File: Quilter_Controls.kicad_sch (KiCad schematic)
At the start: 16 parts, among them J1 Conn_01x10_Male, J10 Conn_01x04_Male, J2 Conn_01x10_Male, J3 Conn_01x10_Male, J4 Audio_In, J5 Audio_Out, J6 Audio_Mix, J7 Freq_V_Oct, J8 Freq_CV, J9 Conn_02x04_Top_Bottom

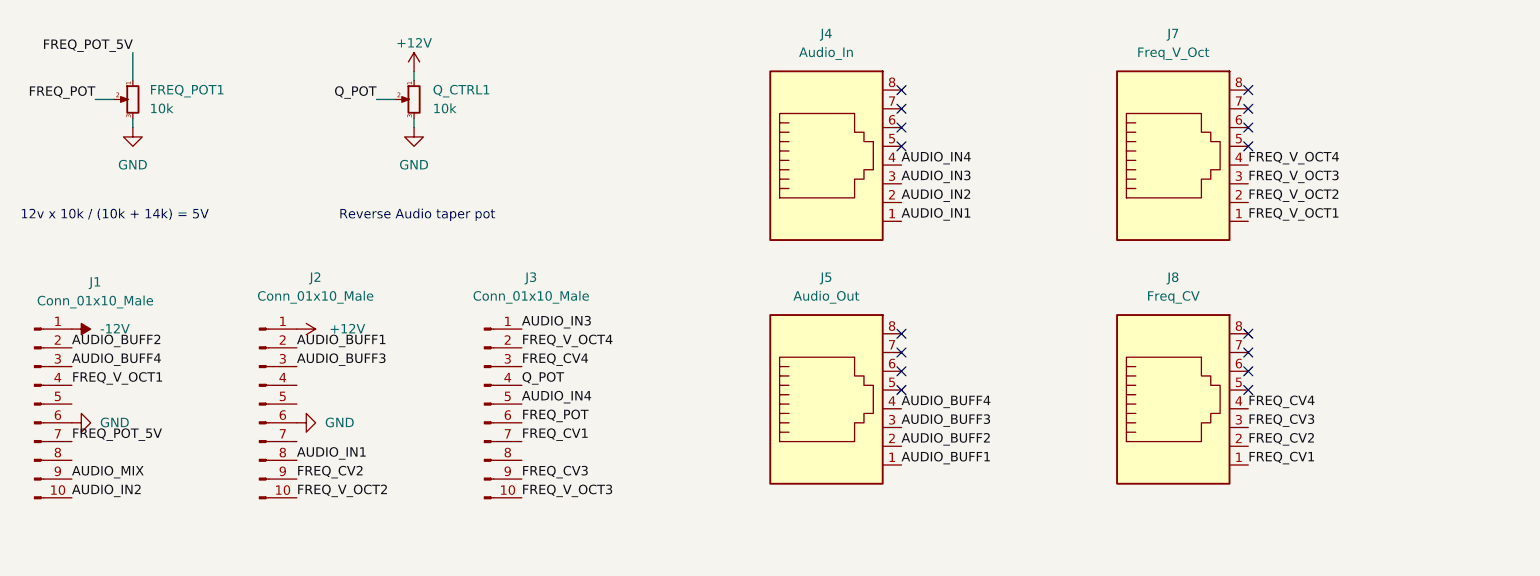
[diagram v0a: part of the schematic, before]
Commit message: Added all voice filter CV; panel draft done
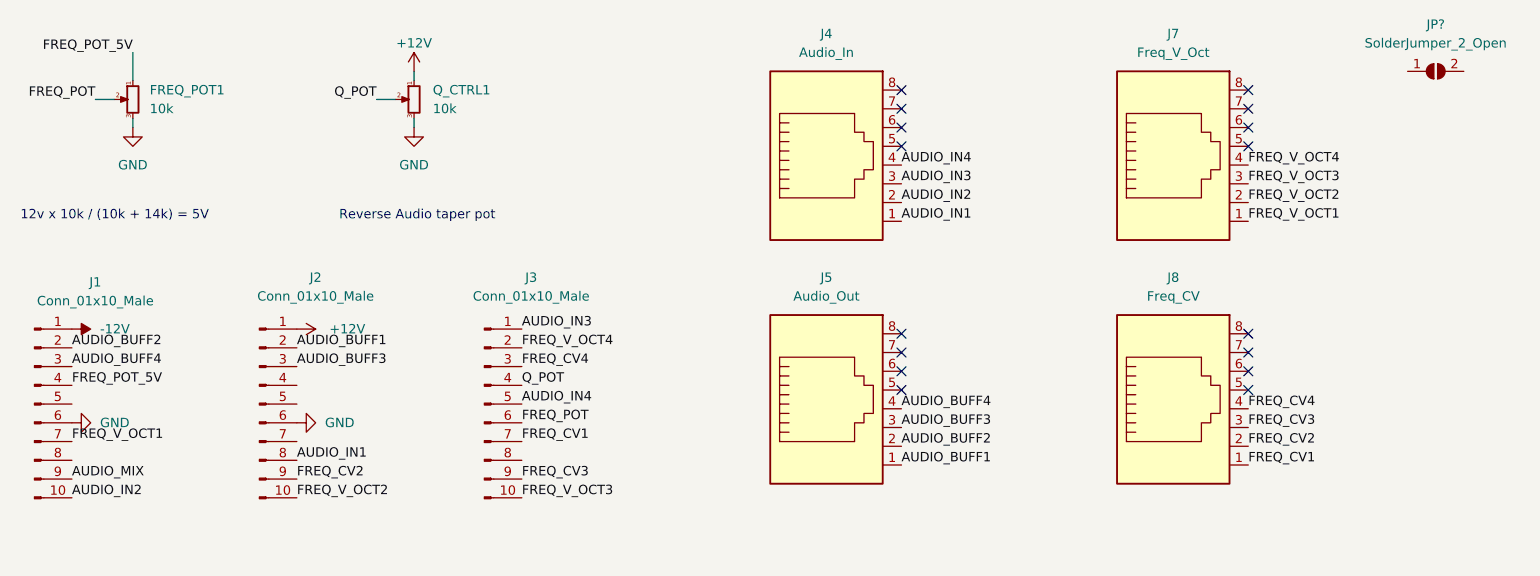
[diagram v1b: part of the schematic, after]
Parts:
- added JP?: SolderJumper_2_Open, symbol Jumper:SolderJumper_2_Open
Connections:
- net FREQ_POT_5V: now also J1.4 (Pin_4); no longer J1.7 (Pin_7)
- net FREQ_V_OCT1: now also J1.7 (Pin_7); no longer J1.4 (Pin_4)
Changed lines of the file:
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@@
     (effects (font (size 1.27 1.27)) (justify left bottom))
   )
-  (label "FREQ_V_OCT1" (at 32.385 74.295 0)
+  (label "FREQ_V_OCT1" (at 32.385 81.915 0)
     (effects (font (size 1.27 1.27)) (justify left bottom))
   )
@@
     (effects (font (size 1.27 1.27)) (justify left bottom))
   )
-  (label "FREQ_POT_5V" (at 32.385 81.915 0)
+  (label "FREQ_POT_5V" (at 32.385 74.295 0)
     (effects (font (size 1.27 1.27)) (justify left bottom))
   )
@@
     (pin "1")
   )
+  (symbol (lib_id "Jumper:SolderJumper_2_Open") (at 217.17 31.75 0) (unit 1)
+    (in_bom yes) (on_board yes) (fields_autoplaced)
+    (property "Reference" "JP?" (id 0) (at 217.17 25.4 0))
+    (property "Value" "SolderJumper_2_Open" (id 1) (at 217.17 27.94 0))
+    (property "Footprint" "" (id 2) (at 217.17 31.75 0)
+      (effects (font (size 1.27 1.27)) hide)
+    )
+    (property "Datasheet" "~" (id 3) (at 217.17 31.75 0)
+      (effects (font (size 1.27 1.27)) hide)
+    )
+    (pin "1")
+    (pin "2")
+  )
   (symbol (lib_id "Connector:RJ45") (at 181.61 77.47 0) (unit 1)
     (in_bom yes) (on_board yes) (fields_autoplaced)
@@
       (reference "J10") (unit 1) (value "Conn_01x04_Male") (footprint "Connector_PinHeader_2.54mm:PinHeader_1x04_P2.54mm_Vertical")
     )
+    (path "/d77a8722-4bb4-4880-a6c4-c869695b03b3"
+      (reference "JP?") (unit 1) (value "SolderJumper_2_Open") (footprint "")
+    )
     (path "/f38c0160-bb84-444d-8a78-a30a89498250"

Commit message: Updates to panel and component boards
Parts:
- added J11: Freq_In, Custom_Footprints:THONKICONN_hole, symbol thonkiconn:AudioJack2_Ground_Switch
- JP1: renamed from JP?; now left out of the parts list
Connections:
- net GND: now also J11.1, J11.2
- net FREQ_JACK: now reaches J3.8 (Pin_8)
- net FREQ_JACK: now also J11.3
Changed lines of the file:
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@@
 (kicad_sch (version 20211123) (generator eeschema)
   (paper "A4")
+  (junction (at 109.22 129.54) (diameter 0) (color 0 0 0 0)
+  )
   (no_connect (at 144.78 41.91))
   (no_connect (at 144.78 36.83))
@@
     (stroke (width 0) (type default) (color 0 0 0 0))
   )
+  (wire (pts (xy 109.22 129.54) (xy 109.22 133.35))
+    (stroke (width 0) (type default) (color 0 0 0 0))
+  )
   (wire (pts (xy 78.74 39.37) (xy 78.74 38.1))
     (stroke (width 0) (type default) (color 0 0 0 0))
   )
+  (wire (pts (xy 106.68 129.54) (xy 109.22 129.54))
+    (stroke (width 0) (type default) (color 0 0 0 0))
+  )
+  (wire (pts (xy 106.68 124.46) (xy 109.22 124.46))
+    (stroke (width 0) (type default) (color 0 0 0 0))
+  )
+  (wire (pts (xy 106.68 127) (xy 111.76 127))
+    (stroke (width 0) (type default) (color 0 0 0 0))
+  )
   (wire (pts (xy 139.7 124.46) (xy 142.24 124.46))
     (stroke (width 0) (type default) (color 0 0 0 0))
@@
   )
   (wire (pts (xy 78.74 33.02) (xy 78.74 31.75))
+    (stroke (width 0) (type default) (color 0 0 0 0))
+  )
+  (wire (pts (xy 109.22 124.46) (xy 109.22 129.54))
     (stroke (width 0) (type default) (color 0 0 0 0))
   )
@@
     (effects (font (size 1.27 1.27)) (justify left bottom))
   )
+  (label "FREQ_JACK" (at 93.345 84.455 0)
+    (effects (font (size 1.27 1.27)) (justify left bottom))
+  )
   (label "AUDIO_IN2" (at 101.6 159.385 180)
     (effects (font (size 1.27 1.27)) (justify right bottom))
@@
   )
   (label "AUDIO_IN2" (at 32.385 89.535 0)
+    (effects (font (size 1.27 1.27)) (justify left bottom))
+  )
+  (label "FREQ_JACK" (at 111.76 127 0)
     (effects (font (size 1.27 1.27)) (justify left bottom))
   )
@@
     (pin "8")
   )
+  (symbol (lib_id "thonkiconn:AudioJack2_Ground_Switch") (at 101.6 127 0) (unit 1)
+    (in_bom yes) (on_board yes) (fields_autoplaced)
+    (property "Reference" "J11" (id 0) (at 100.33 116.84 0))
+    (property "Value" "Freq_In" (id 1) (at 100.33 119.38 0))
+    (property "Footprint" "Custom_Footprints:THONKICONN_hole" (id 2) (at 101.6 127 0)
+      (effects (font (size 1.27 1.27)) hide)
+    )
+    (property "Datasheet" "~" (id 3) (at 101.6 127 0)
+      (effects (font (size 1.27 1.27)) hide)
+    )
+    (pin "1")
+    (pin "2")
+    (pin "3")
+  )
   (symbol (lib_id "power:+12V") (at 78.74 31.75 0) (mirror y) (unit 1)
     (in_bom yes) (on_board yes)
@@
     (pin "1")
   )
+  (symbol (lib_id "power:GND") (at 109.22 133.35 0) (unit 1)
+    (in_bom yes) (on_board yes)
+    (property "Reference" "#PWR02" (id 0) (at 109.22 139.7 0)
+      (effects (font (size 1.27 1.27)) hide)
+    )
+    (property "Value" "GND" (id 1) (at 109.347 137.7442 0))
+    (property "Footprint" "" (id 2) (at 109.22 133.35 0)
+      (effects (font (size 1.27 1.27)) hide)
+    )
+    (property "Datasheet" "" (id 3) (at 109.22 133.35 0)
+      (effects (font (size 1.27 1.27)) hide)
+    )
+    (pin "1")
+  )
   (symbol (lib_id "power:+12V") (at 45.72 157.48 90) (mirror x) (unit 1)
     (in_bom yes) (on_board yes) (fields_autoplaced)
@@
   )
   (symbol (lib_id "Jumper:SolderJumper_2_Open") (at 217.17 31.75 0) (unit 1)
-    (in_bom yes) (on_board yes) (fields_autoplaced)
-    (property "Reference" "JP?" (id 0) (at 217.17 25.4 0))
+    (in_bom no) (on_board no) (fields_autoplaced)
+    (property "Reference" "JP1" (id 0) (at 217.17 25.4 0))
     (property "Value" "SolderJumper_2_Open" (id 1) (at 217.17 27.94 0))
     (property "Footprint" "" (id 2) (at 217.17 31.75 0)
@@
       (reference "#PWR01") (unit 1) (value "GND") (footprint "")
     )
+    (path "/7f9f9f35-3cdd-4c03-90f1-60407f96b2b7"
+      (reference "#PWR02") (unit 1) (value "GND") (footprint "")
+    )
     (path "/821b4764-59ef-462b-8f4f-a2b957a29821"
       (reference "#PWR04") (unit 1) (value "+12V") (footprint "")
@@
       (reference "J10") (unit 1) (value "Conn_01x04_Male") (footprint "Connector_PinHeader_2.54mm:PinHeader_1x04_P2.54mm_Vertical")
     )
+    (path "/48c3acd2-f2de-4423-8518-5c599445cb96"
+      (reference "J11") (unit 1) (value "Freq_In") (footprint "Custom_Footprints:THONKICONN_hole")
+    )
     (path "/d77a8722-4bb4-4880-a6c4-c869695b03b3"
-      (reference "JP?") (unit 1) (value "SolderJumper_2_Open") (footprint "")
+      (reference "JP1") (unit 1) (value "SolderJumper_2_Open") (footprint "")
     )
     (path "/f38c0160-bb84-444d-8a78-a30a89498250"

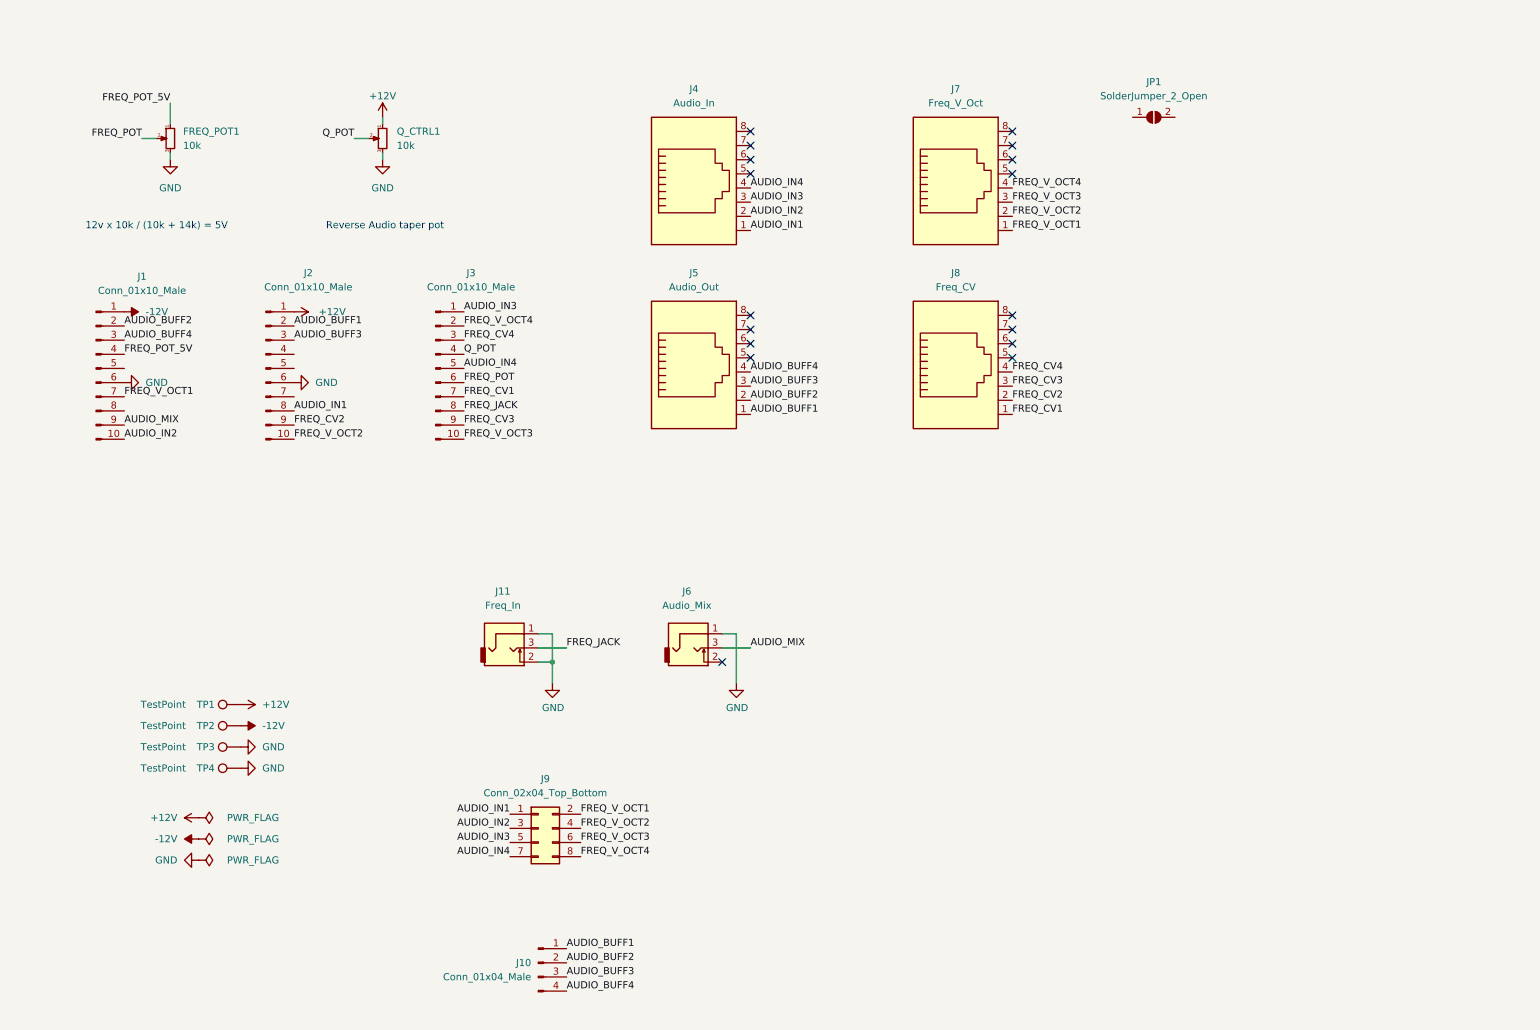
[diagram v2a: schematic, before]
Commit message: Finished routing components and controls
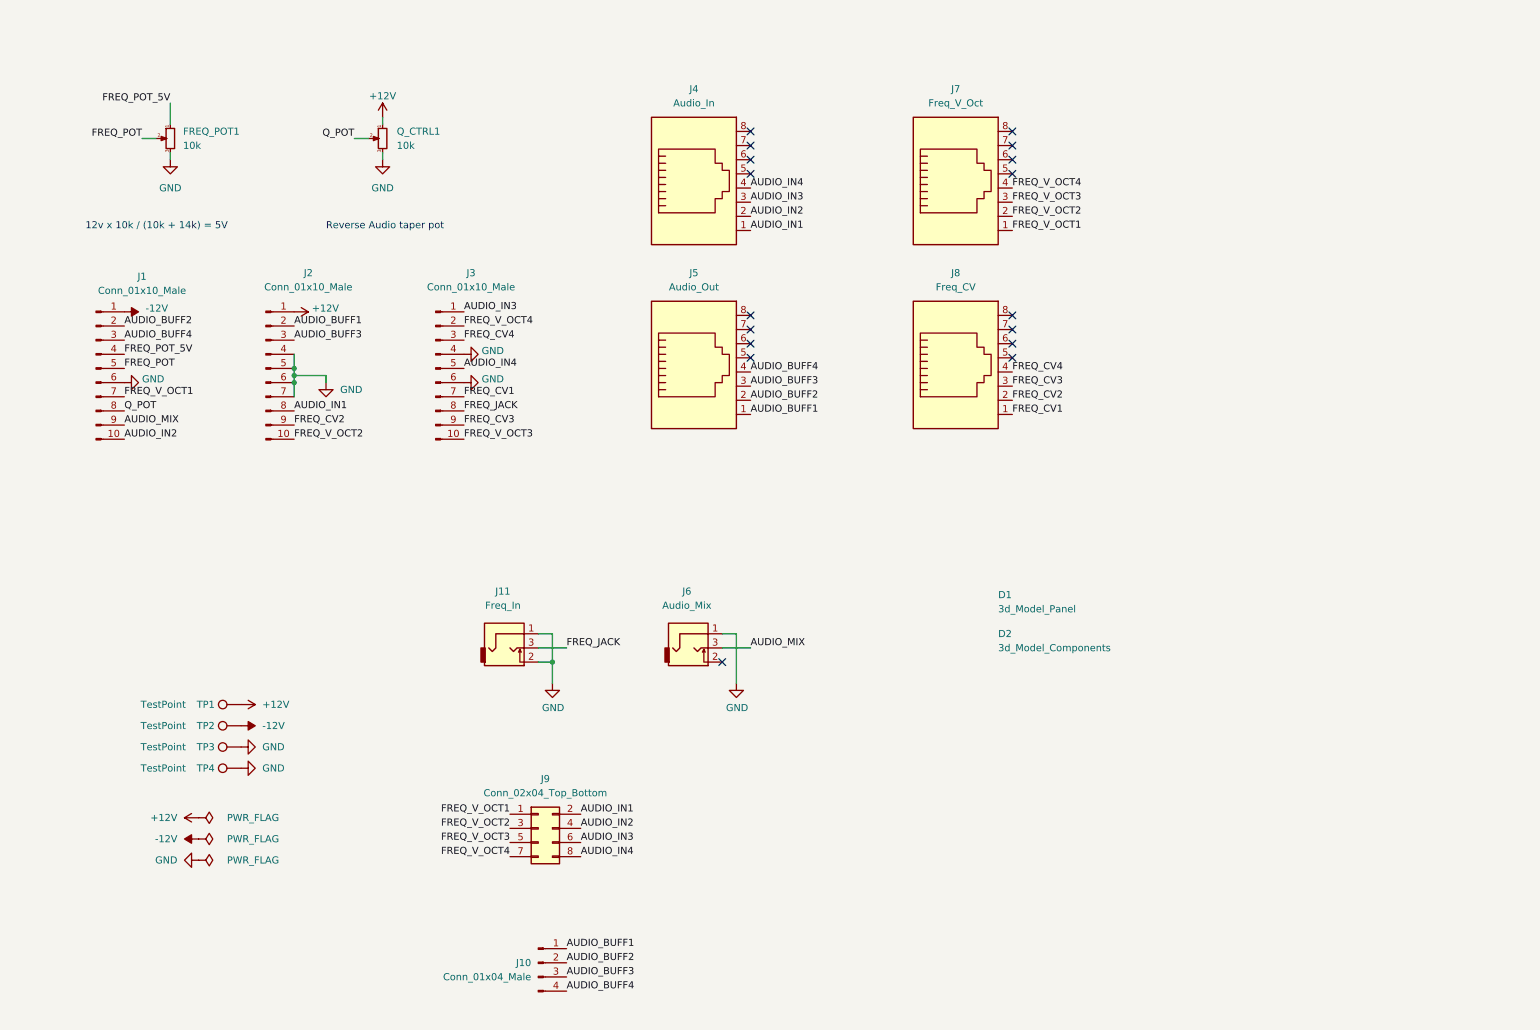
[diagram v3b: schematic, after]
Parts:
- removed JP1: SolderJumper_2_Open, symbol Jumper:SolderJumper_2_Open
- added D1: 3d_Model_Panel, Custom_Footprints:3D_Dummy, symbol Mountjoy:3d_Model_Dummy
- added D2: 3d_Model_Components, Custom_Footprints:3D_Dummy, symbol Mountjoy:3d_Model_Dummy
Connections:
- net AUDIO_IN1: now also J9.2 (Pin_2); no longer J9.1 (Pin_1)
- net AUDIO_IN2: now also J9.4 (Pin_4); no longer J9.3 (Pin_3)
- net AUDIO_IN3: now also J9.6 (Pin_6); no longer J9.5 (Pin_5)
- net AUDIO_IN4: now also J9.8 (Pin_8); no longer J9.7 (Pin_7)
- net FREQ_POT: now also J1.5 (Pin_5); no longer J3.6 (Pin_6)
- net FREQ_V_OCT1: now also J9.1 (Pin_1); no longer J9.2 (Pin_2)
- net FREQ_V_OCT2: now also J9.3 (Pin_3); no longer J9.4 (Pin_4)
- net FREQ_V_OCT3: now also J9.5 (Pin_5); no longer J9.6 (Pin_6)
- net FREQ_V_OCT4: now also J9.7 (Pin_7); no longer J9.8 (Pin_8)
- net GND: now also J2.4 (Pin_4), J2.5 (Pin_5), J2.7 (Pin_7), J3.4 (Pin_4), J3.6 (Pin_6)
- net Q_POT: now also J1.8 (Pin_8); no longer J3.4 (Pin_4)

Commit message: Schematic formatting
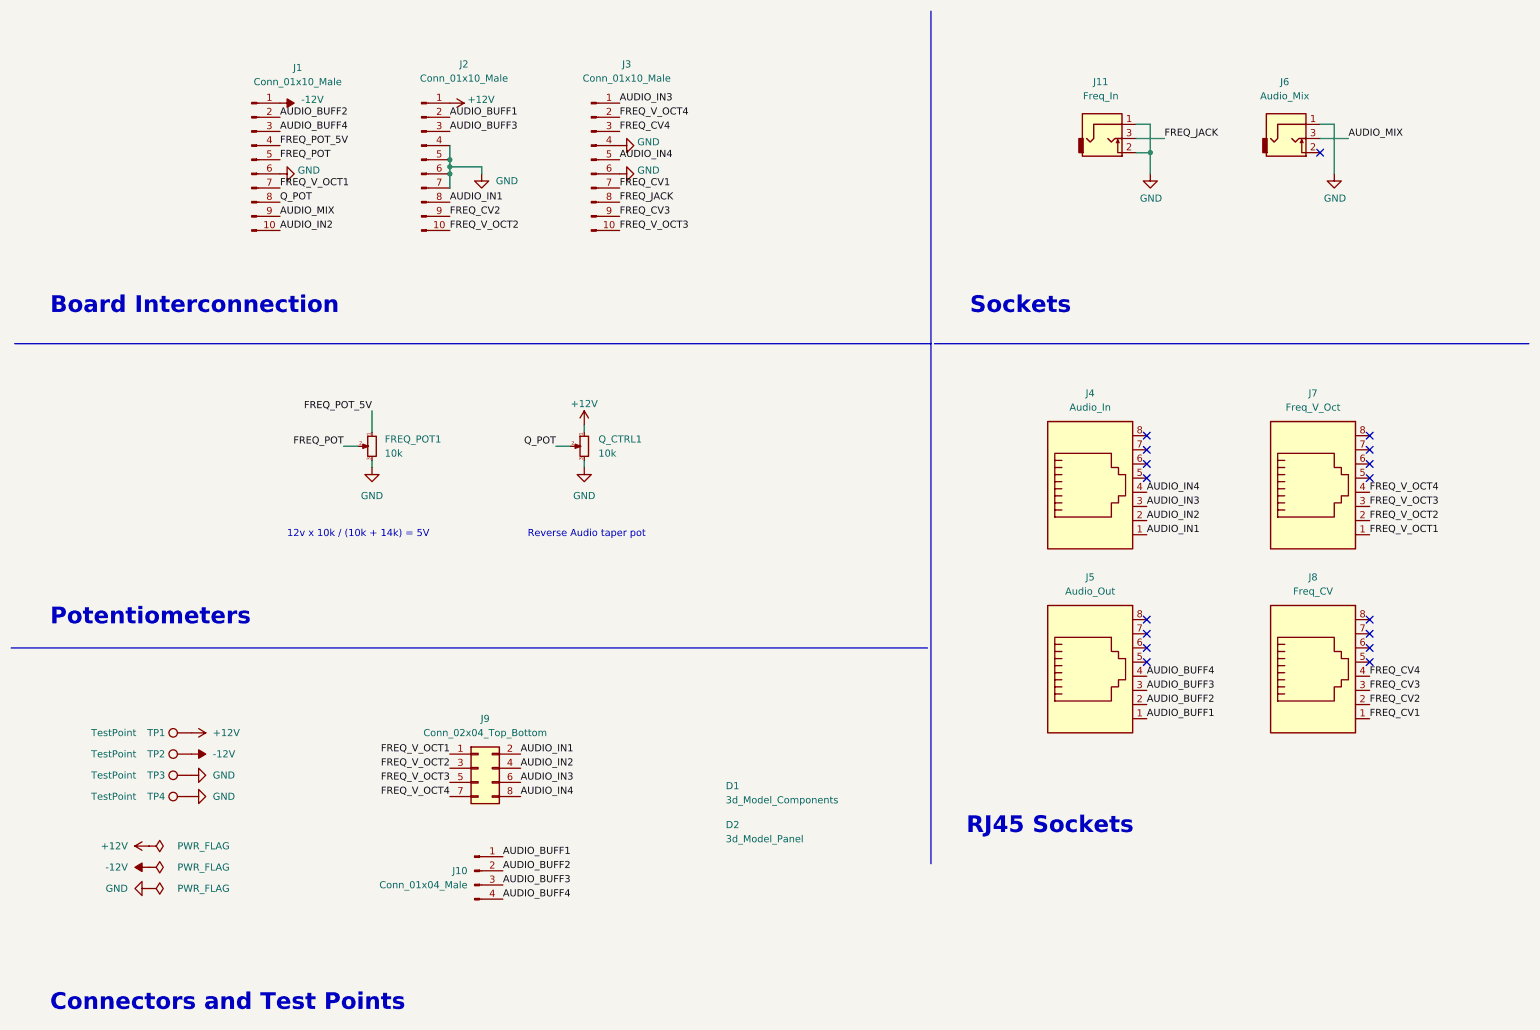
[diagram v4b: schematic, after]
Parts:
- D1: value 3d_Model_Panel -> 3d_Model_Components
- D2: value 3d_Model_Components -> 3d_Model_Panel
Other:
- note added: "Board Interconnection"
- note added: "Connectors and Test Points"
- note added: "Potentiometers"
- note added: "RJ45 Sockets"
- note added: "Sockets"
- moved on the sheet: FREQ_POT1, J1, J10, J11, J2, J3, J4, J5, J6, J7, J8, J9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
